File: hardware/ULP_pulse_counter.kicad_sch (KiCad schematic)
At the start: 9 parts, among them Q1 TEPT4400, SW1 SW_Push, SW2 SW_SPST, U1 XIAO-ESP32-S3-SMD

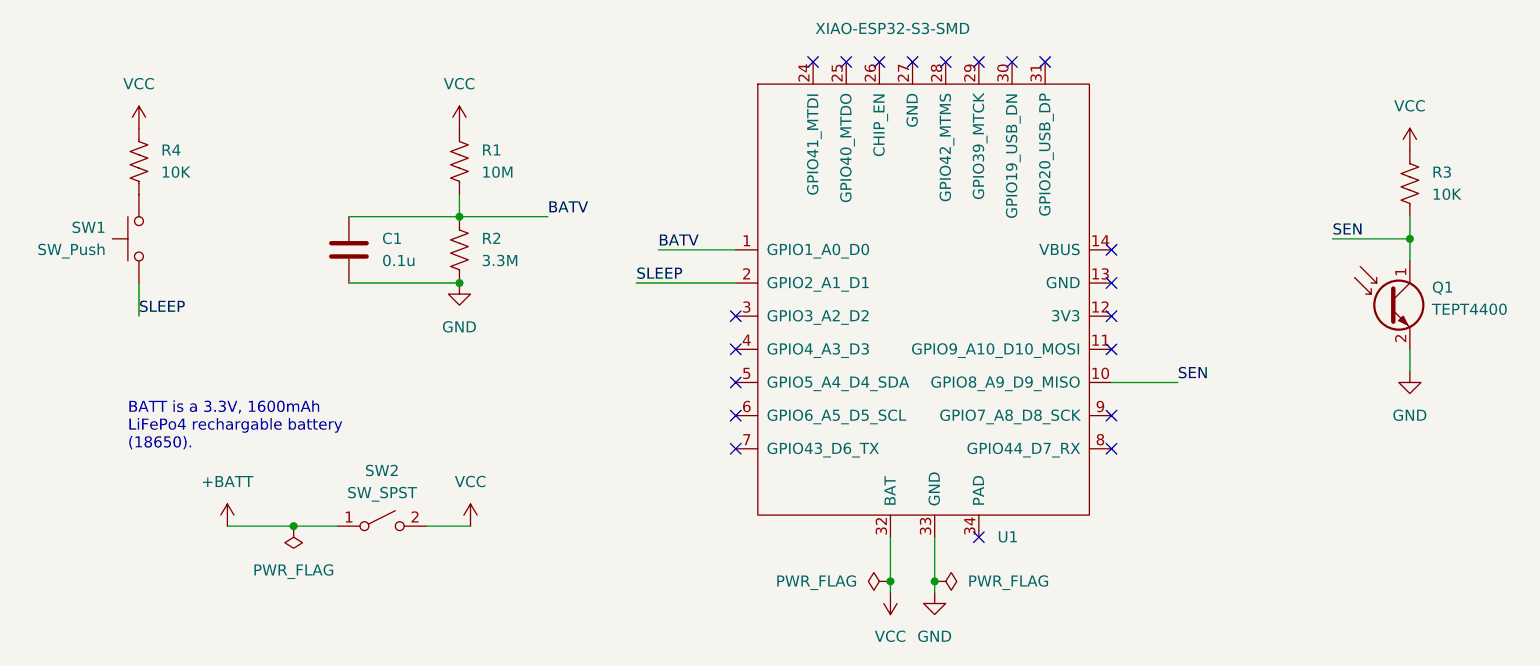
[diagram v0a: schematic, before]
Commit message: Small schematic update
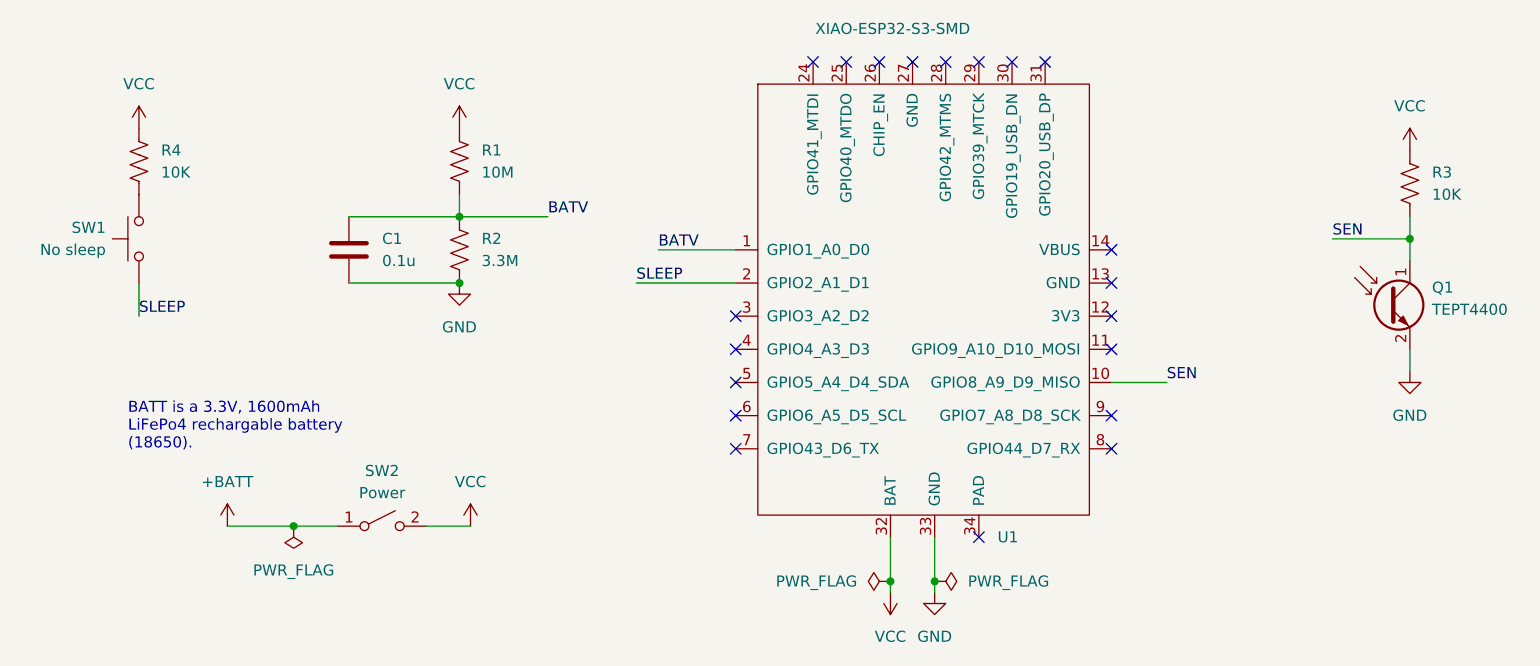
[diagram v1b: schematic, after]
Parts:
- SW1: value SW_Push -> No sleep
- SW2: value SW_SPST -> Power
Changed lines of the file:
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@@
 	(wire
 		(pts
-			(xy 143.51 57.15) (xy 151.13 57.15)
+			(xy 143.51 57.15) (xy 149.86 57.15)
 		)
 		(stroke
@@
 	)
 	(label "SEN"
-		(at 151.13 57.15 0)
+		(at 149.86 57.15 0)
 		(effects
 			(font
@@
 			)
 		)
-		(property "Value" "SW_SPST"
+		(property "Value" "Power"
 			(at 59.69 69.85 0)
 			(show_name no)
@@
 			)
 		)
-		(property "Value" "SW_Push"
+		(property "Value" "No sleep"
 			(at 27.94 41.9099 90)
 			(show_name no)
